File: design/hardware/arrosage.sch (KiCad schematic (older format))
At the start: 8 parts, among them J1 Jack-DC, Q1 TIP120, SW1 SW_Push, SW2 SW_Push, U1 Pololu_A-Star_328PB_Micro

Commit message: plus de design
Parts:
- added D1: DIODE, symbol pspice:DIODE
- added MS1: Moisture_Sensor, symbol arrosage-rescue:Moisture_Sensor-Comp
- U1: symbol Comp:Pololu_A-Star_328PB_Micro -> arrosage-rescue:Pololu_A-Star_328PB_Micro-Comp
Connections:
- net labels removed: SENSOR+, SENSOR-, SENSOR_A0, SENSOR_D0
- wire segments 49 -> 54
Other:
- moved on the sheet: J1
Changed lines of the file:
@@
 L Connector:Jack-DC J1
 U 1 1 61733C01
-P 9350 1750
-F 0 "J1" H 9407 2075 50  0000 C CNN
-F 1 "Jack-DC" H 9407 1984 50  0000 C CNN
-F 2 "" H 9400 1710 50  0001 C CNN
-F 3 "~" H 9400 1710 50  0001 C CNN
-	1    9350 1750
+P 9400 1750
+F 0 "J1" H 9457 2075 50  0000 C CNN
+F 1 "Jack-DC" H 9457 1984 50  0000 C CNN
+F 2 "" H 9450 1710 50  0001 C CNN
+F 3 "~" H 9450 1710 50  0001 C CNN
+	1    9400 1750
 	-1   0    0    1
 $EndComp
@@
 	4150 3050 4600 3050
 $Comp
-L Comp:Pololu_A-Star_328PB_Micro U1
+L arrosage-rescue:Pololu_A-Star_328PB_Micro-Comp U1
 U 1 1 617307EC
 P 5200 2350
@@
 	1    0    0    -1
 $EndComp
-Wire Wire Line
-	8300 3400 7850 3400
-Wire Wire Line
-	8300 4150 7850 4150
 Connection ~ 7850 3400
 Wire Wire Line
@@
 $EndComp
 Wire Wire Line
-	9050 1850 8750 1850
-Wire Wire Line
-	6250 1850 6250 2650
+	9100 1850 8850 1850
+Wire Wire Line
+	6300 1850 6300 2650
 Wire Wire Line
 	6050 4500 6050 3800
 Wire Wire Line
-	8750 1850 8750 4800
-Wire Wire Line
-	8750 4800 7850 4800
-Connection ~ 8750 1850
-Wire Wire Line
-	8750 1850 6250 1850
+	8850 1850 8850 4800
+Wire Wire Line
+	8850 4800 7850 4800
+Connection ~ 8850 1850
+Wire Wire Line
+	8850 1850 6300 1850
 Connection ~ 7850 4150
 Wire Wire Line
@@
 Wire Wire Line
 	6050 3800 7050 3800
-Wire Wire Line
-	3650 4800 7850 4800
 Connection ~ 7850 4800
 Wire Wire Line
 	7850 4800 7850 4150
-Wire Wire Line
-	6050 1650 7850 1650
 Wire Wire Line
 	7850 1650 7850 3400
 Connection ~ 7850 1650
 Wire Wire Line
-	7850 1650 9050 1650
+	7850 1650 8850 1650
 Wire Wire Line
 	5400 3450 6300 3450
 Wire Wire Line
-	6300 3450 6300 3000
-Wire Wire Line
-	6300 3000 6850 3000
-Wire Wire Line
 	5400 3550 6550 3550
-Wire Wire Line
-	6550 3550 6550 3200
-Wire Wire Line
-	6550 3200 6850 3200
-Wire Wire Line
-	6250 2650 6850 2650
-Wire Wire Line
-	6850 2800 5700 2800
-Wire Wire Line
-	5700 2800 5700 2750
-Wire Wire Line
-	5700 2750 5400 2750
 Wire Wire Line
 	4150 2500 4100 2500
@@
 NoConn ~ 4600 2650
 NoConn ~ 4600 2550
-Text Label 7300 2700 2    50   ~ 0
-SENSOR-
-Text Label 7300 2850 2    50   ~ 0
-SENSOR+
-Text Label 7350 3050 2    50   ~ 0
-SENSOR_A0
-Text Label 7350 3250 2    50   ~ 0
-SENSOR_D0
-Text Label 8650 3450 2    50   ~ 0
+Text Label 8750 3450 2    50   ~ 0
 VALVE1
-Text Label 8650 4200 2    50   ~ 0
+Text Label 8750 4200 2    50   ~ 0
 VALVE2
 Wire Wire Line
 	5400 2550 6050 2550
 Wire Wire Line
-	5400 2650 6250 2650
-Connection ~ 6250 2650
+	5400 2650 6300 2650
+$Comp
+L pspice:DIODE D1
+U 1 1 6173D2A8
+P 8350 3800
+F 0 "D1" V 8396 3672 50  0000 R CNN
+F 1 "DIODE" V 8305 3672 50  0000 R CNN
+F 2 "" H 8350 3800 50  0001 C CNN
+F 3 "~" H 8350 3800 50  0001 C CNN
+	1    8350 3800
+	0    -1   -1   0
+$EndComp
+Wire Wire Line
+	8350 3600 8350 3400
+Wire Wire Line
+	7850 3400 8350 3400
+Wire Wire Line
+	8350 3400 8450 3400
+Connection ~ 8350 3400
+Wire Wire Line
+	8350 4000 8350 4150
+Wire Wire Line
+	7850 4150 8350 4150
+Wire Wire Line
+	8350 4150 8450 4150
+Connection ~ 8350 4150
+$Comp
+L arrosage-rescue:Moisture_Sensor-Comp MS1
+U 1 1 61742CA5
+P 7250 2550
+F 0 "MS1" H 7778 2251 50  0000 L CNN
+F 1 "Moisture_Sensor" H 7778 2160 50  0000 L CNN
+F 2 "" H 7300 2450 50  0001 C CNN
+F 3 "" H 7300 2450 50  0001 C CNN
+	1    7250 2550
+	1    0    0    -1
+$EndComp
+Connection ~ 6300 2650
+Wire Wire Line
+	6300 2950 6800 2950
+Wire Wire Line
+	6300 2950 6300 3450
+Wire Wire Line
+	6550 3050 6800 3050
+Wire Wire Line
+	6550 3050 6550 3550
+Wire Wire Line
+	5400 2750 6650 2750
+Wire Wire Line
+	6300 2650 6300 2850
+Wire Wire Line
+	6300 2850 6800 2850
+Wire Wire Line
+	6050 1650 7850 1650
+Wire Wire Line
+	3650 4800 7850 4800
+$Comp
+L power:PWR_FLAG #FLG0101
+U 1 1 617493FA
+P 8850 1650
+F 0 "#FLG0101" H 8850 1725 50  0001 C CNN
+F 1 "PWR_FLAG" H 8850 1823 50  0000 C CNN
+F 2 "" H 8850 1650 50  0001 C CNN
+F 3 "~" H 8850 1650 50  0001 C CNN
+	1    8850 1650
+	1    0    0    -1
+$EndComp
+Connection ~ 8850 1650
+Wire Wire Line
+	8850 1650 9100 1650
+$Comp
+L power:PWR_FLAG #FLG0102
+U 1 1 61749ACF
+P 6650 2750
+F 0 "#FLG0102" H 6650 2825 50  0001 C CNN
+F 1 "PWR_FLAG" H 6650 2923 50  0000 C CNN
+F 2 "" H 6650 2750 50  0001 C CNN
+F 3 "~" H 6650 2750 50  0001 C CNN
+	1    6650 2750
+	1    0    0    -1
+$EndComp
+Connection ~ 6650 2750
+Wire Wire Line
+	6650 2750 6800 2750
 $EndSCHEMATC

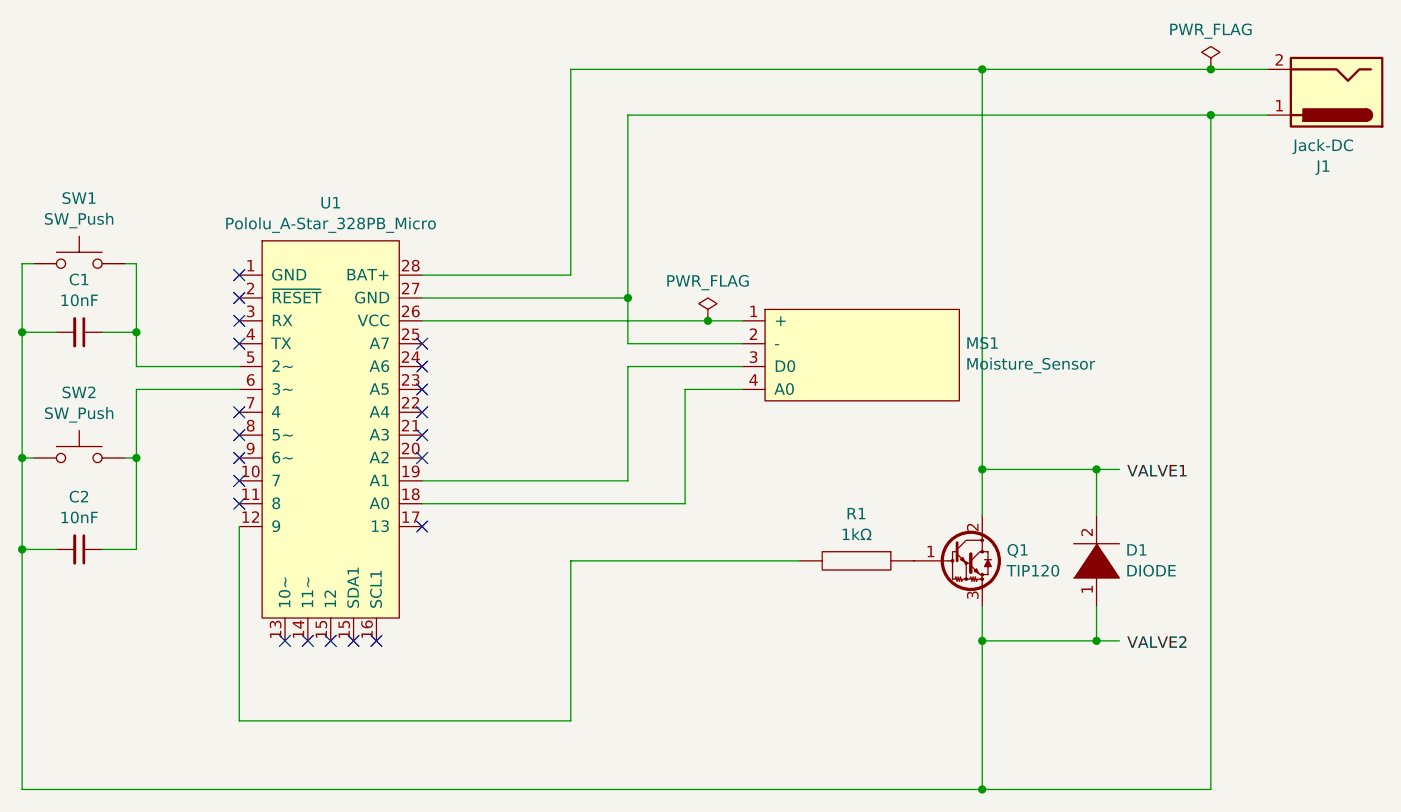
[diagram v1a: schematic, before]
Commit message: correction du schéma électrique
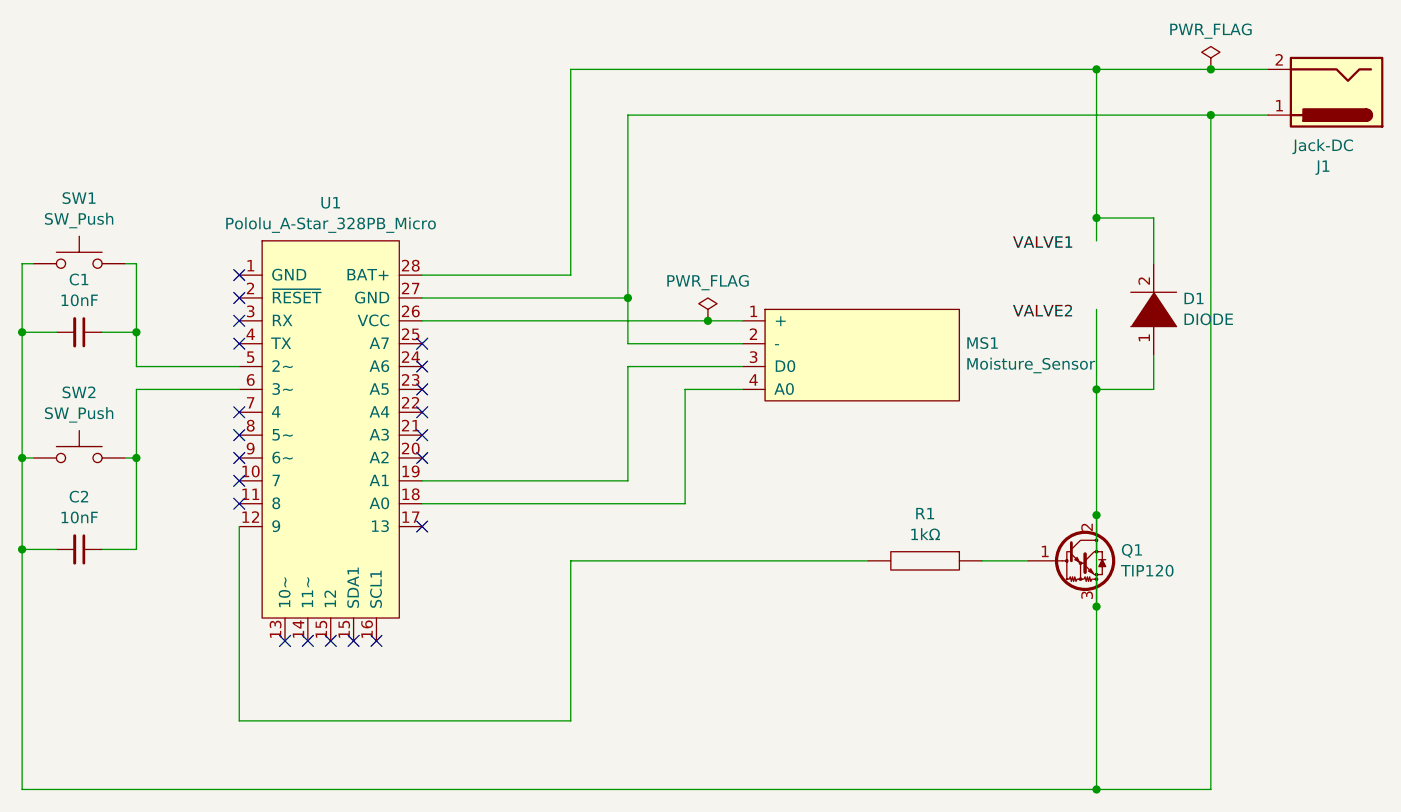
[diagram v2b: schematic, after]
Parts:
- U1: footprint (none) -> Module:Pololu_Breakout-16_15.2x20.3mm
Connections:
- wire segments 54 -> 55
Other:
- moved on the sheet: D1, Q1, R1
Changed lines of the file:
@@
 F 0 "U1" H 5000 2465 50  0000 C CNN
 F 1 "Pololu_A-Star_328PB_Micro" H 5000 2374 50  0000 C CNN
-F 2 "" H 4750 2250 50  0001 C CNN
+F 2 "Module:Pololu_Breakout-16_15.2x20.3mm" H 4750 2250 50  0001 C CNN
 F 3 "" H 4750 2250 50  0001 C CNN
 	1    5200 2350
 	1    0    0    -1
 $EndComp
-Connection ~ 7850 3400
-Wire Wire Line
-	7850 4000 7850 4150
-Wire Wire Line
-	7850 3600 7850 3400
 $Comp
 L Transistor_BJT:TIP120 Q1
 U 1 1 61743178
-P 7750 3800
-F 0 "Q1" H 7957 3846 50  0000 L CNN
-F 1 "TIP120" H 7957 3755 50  0000 L CNN
-F 2 "Package_TO_SOT_THT:TO-220-3_Vertical" H 7950 3725 50  0001 L CIN
-F 3 "https://www.onsemi.com/pub/Collateral/TIP120-D.PDF" H 7750 3800 50  0001 L CNN
-	1    7750 3800
+P 8250 3800
+F 0 "Q1" H 8457 3846 50  0000 L CNN
+F 1 "TIP120" H 8457 3755 50  0000 L CNN
+F 2 "Package_TO_SOT_THT:TO-220-3_Vertical" H 8450 3725 50  0001 L CIN
+F 3 "https://www.onsemi.com/pub/Collateral/TIP120-D.PDF" H 8250 3800 50  0001 L CNN
+	1    8250 3800
 	1    0    0    -1
 $EndComp
@@
 	8850 1850 8850 4800
 Wire Wire Line
-	8850 4800 7850 4800
+	8850 4800 8350 4800
 Connection ~ 8850 1850
 Wire Wire Line
 	8850 1850 6300 1850
-Connection ~ 7850 4150
 Wire Wire Line
 	4600 2950 4150 2950
@@
 L pspice:R R1
 U 1 1 6175D80B
-P 7300 3800
-F 0 "R1" V 7095 3800 50  0000 C CNN
-F 1 "1kΩ" V 7186 3800 50  0000 C CNN
-F 2 "" H 7300 3800 50  0001 C CNN
-F 3 "~" H 7300 3800 50  0001 C CNN
-	1    7300 3800
+P 7600 3800
+F 0 "R1" V 7395 3800 50  0000 C CNN
+F 1 "1kΩ" V 7486 3800 50  0000 C CNN
+F 2 "" H 7600 3800 50  0001 C CNN
+F 3 "~" H 7600 3800 50  0001 C CNN
+	1    7600 3800
 	0    1    1    0
 $EndComp
@@
 	3650 3750 3650 4800
 Wire Wire Line
-	6050 3800 7050 3800
-Connection ~ 7850 4800
-Wire Wire Line
-	7850 4800 7850 4150
-Wire Wire Line
-	7850 1650 7850 3400
-Connection ~ 7850 1650
-Wire Wire Line
-	7850 1650 8850 1650
+	6050 3800 7350 3800
 Wire Wire Line
 	5400 3450 6300 3450
@@
 NoConn ~ 4600 2650
 NoConn ~ 4600 2550
-Text Label 8750 3450 2    50   ~ 0
+Text Label 8250 2450 2    50   ~ 0
 VALVE1
-Text Label 8750 4200 2    50   ~ 0
+Text Label 8250 2750 2    50   ~ 0
 VALVE2
 Wire Wire Line
@@
 L pspice:DIODE D1
 U 1 1 6173D2A8
-P 8350 3800
-F 0 "D1" V 8396 3672 50  0000 R CNN
-F 1 "DIODE" V 8305 3672 50  0000 R CNN
-F 2 "" H 8350 3800 50  0001 C CNN
-F 3 "~" H 8350 3800 50  0001 C CNN
-	1    8350 3800
+P 8600 2700
+F 0 "D1" V 8646 2572 50  0000 R CNN
+F 1 "DIODE" V 8555 2572 50  0000 R CNN
+F 2 "" H 8600 2700 50  0001 C CNN
+F 3 "~" H 8600 2700 50  0001 C CNN
+	1    8600 2700
 	0    -1   -1   0
 $EndComp
-Wire Wire Line
-	8350 3600 8350 3400
-Wire Wire Line
-	7850 3400 8350 3400
-Wire Wire Line
-	8350 3400 8450 3400
-Connection ~ 8350 3400
-Wire Wire Line
-	8350 4000 8350 4150
-Wire Wire Line
-	7850 4150 8350 4150
-Wire Wire Line
-	8350 4150 8450 4150
-Connection ~ 8350 4150
 $Comp
 L arrosage-rescue:Moisture_Sensor-Comp MS1
@@
 Wire Wire Line
 	6300 2850 6800 2850
-Wire Wire Line
-	6050 1650 7850 1650
-Wire Wire Line
-	3650 4800 7850 4800
 $Comp
 L power:PWR_FLAG #FLG0101
@@
 Wire Wire Line
 	6650 2750 6800 2750
+Wire Wire Line
+	8350 4000 8350 4800
+Wire Wire Line
+	8350 3050 8350 3600
+Connection ~ 8350 4800
+Wire Wire Line
+	3650 4800 8350 4800
+Wire Wire Line
+	7850 3800 8050 3800
+Connection ~ 8350 3600
+Wire Wire Line
+	8350 3600 8350 4000
+Connection ~ 8350 4000
+Wire Wire Line
+	6050 1650 8350 1650
+Wire Wire Line
+	8350 1650 8350 2300
+Connection ~ 8350 1650
+Wire Wire Line
+	8350 1650 8850 1650
+Wire Wire Line
+	8350 2300 8600 2300
+Wire Wire Line
+	8600 2300 8600 2500
+Wire Wire Line
+	8600 2900 8600 3050
+Wire Wire Line
+	8600 3050 8350 3050
+Wire Wire Line
+	8350 2300 8350 2400
+Connection ~ 8350 2300
+Wire Wire Line
+	8350 3050 8350 2700
+Connection ~ 8350 3050
 $EndSCHEMATC
